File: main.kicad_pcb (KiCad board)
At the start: 2 copper layers, 228.6 x 70.6 mm, 132 parts, among them J1 Conn_02x16_Row_Letter_First, J2 Conn_01x06, J3 Conn_01x02, J4 Screw_Terminal_01x02, J5 Screw_Terminal_01x10, J6 Screw_Terminal_01x10, J7 Screw_Terminal_01x02, J8 Screw_Terminal_01x10, J9 Screw_Terminal_01x10, U1 TPS73233DBVR, U10 TLP222A, U11 TLP222A, U12 TLP222A, U13 TLP222A, U14 TLP222A, U15 TLP222A, U16 TLP222A, U17 TLP222A, U18 TLP222A, U19 TLP222A, U20 TLP222A, U21 TLP222A, U22 TLP222A, U23 TLP222A, U24 TLP222A, U25 TLP222A, U26 TLP3558A, U27 TLP3558A, U28 TLP222A, U29 TLP222A, U3 STM32G070xB, U30 TLP222A, U31 TLP222A, U32 TLP222A, U33 TLP222A, U34 TLP222A, U35 TLP222A, U36 TLP222A, U37 TLP222A, U38 TLP222A, U39 TLP222A, U4 TLP222A, U40 TLP222A, U41 TLP222A, U42 TLP222A, U43 TLP222A, U44 TLP222A, U45 TLP222A, U46 TLP222A, U47 TLP222A, U5 TLP222A, U6 TLP222A, U7 TLP222A, U8 TLP222A, U9 TLP222A

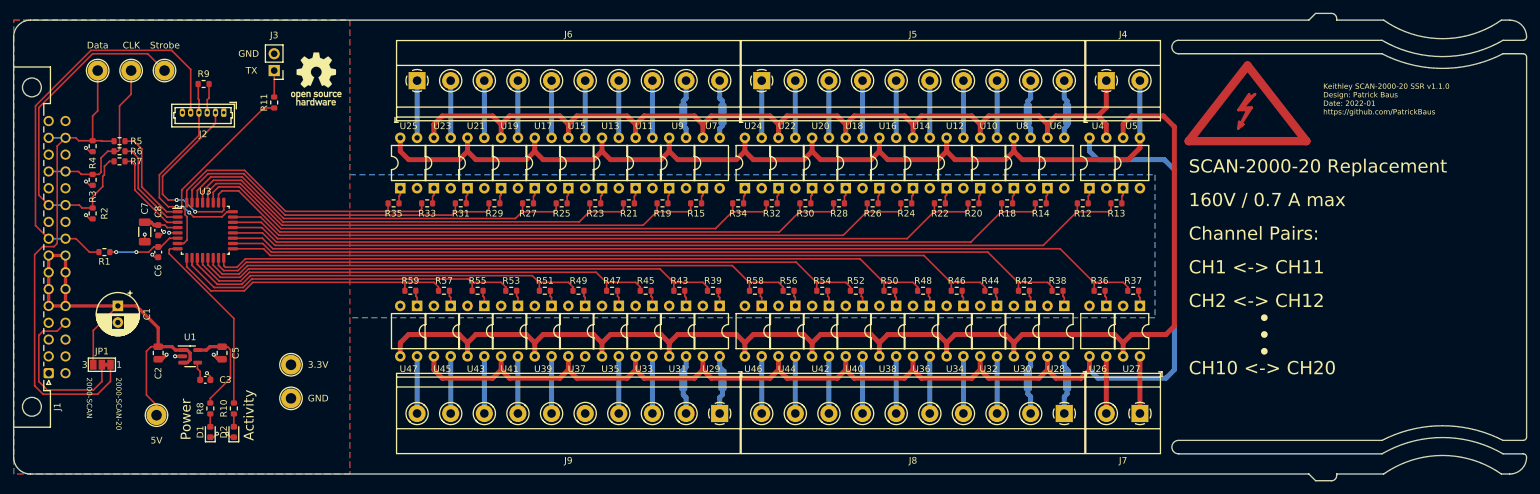
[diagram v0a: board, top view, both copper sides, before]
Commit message: Replaced Picoblade connector with standard pin header Updated libraries to KiCAD 6 format
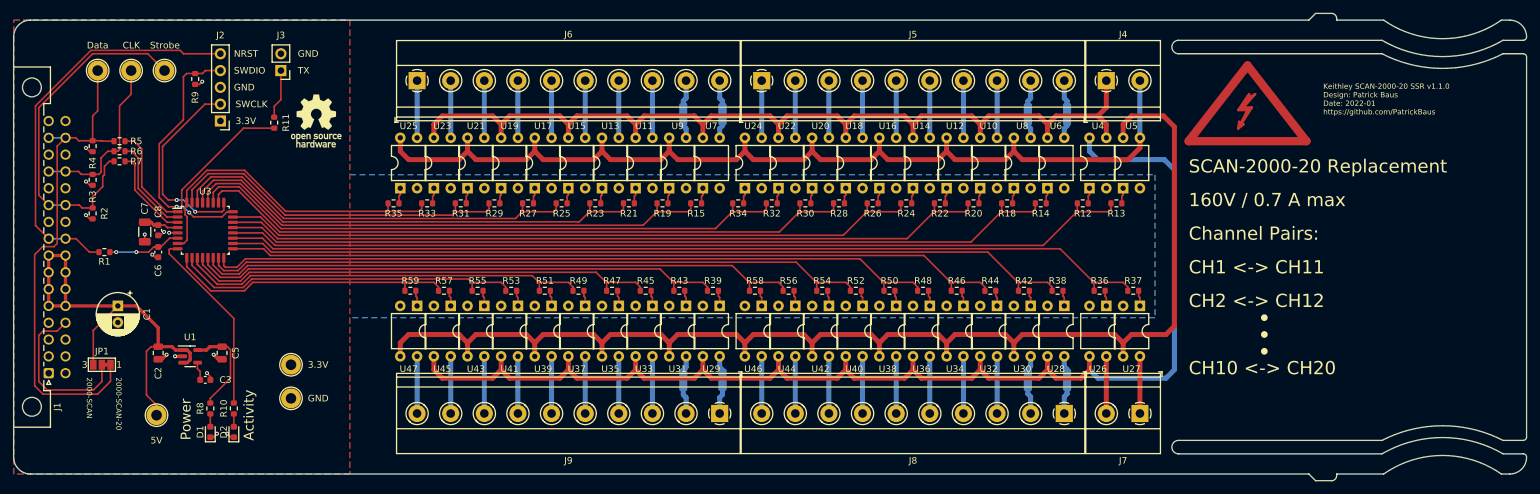
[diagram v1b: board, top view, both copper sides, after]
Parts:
- J2: value Conn_01x06 -> Conn_01x05; footprint Connector_Molex:Molex_PicoBlade_53047-0610_1x06_P1.25mm_Vertical -> Connector_PinHeader_2.54mm:PinHeader_1x05_P2.54mm_Vertical
- moved LOGO2 6.35 mm to (71.1, 63.5)
- moved R11 3.05 mm to (64.8, 63.8)
- moved R9 1.48 mm to (52.8, 57.1), turned to -90 degrees
- moved J2 1.37 mm to (56.6, 63.5)
- moved J3 1.02 mm to (65.8, 55.9)
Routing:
- net Net-(J9-Pad5): track 0.00 -> 8.64 mm
- net /Microcontroller/SWDIO: track 32.3 -> 38.4 mm
- net Net-(J3-Pad1): track 4.00 -> 7.47 mm
- net GND: track 20.7 -> 17.6 mm, vias 13 -> 14
- net /~{NRST}: track 64.0 -> 61.0 mm
- net /Microcontroller/SWCLK: track 27.2 -> 30.2 mm
- net /Microcontroller/TX: track 28.6 -> 27.4 mm
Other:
- board text added: "NRST"
- board text added: "SWCLK"
- board text added: "SWDIO"

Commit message: Updated silkscreen
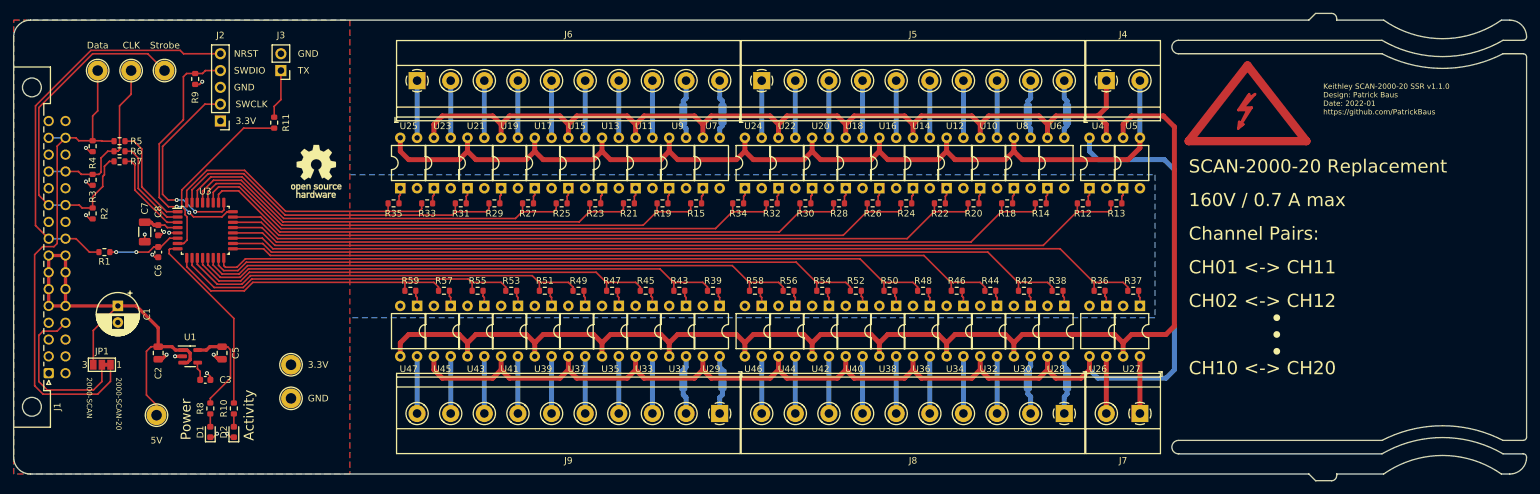
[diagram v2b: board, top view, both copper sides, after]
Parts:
- U3: value STM32G070xB -> STM32G070KBT6
- moved LOGO2 7.62 mm to (71.1, 71.1)
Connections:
- net /Relays/Input pins/In_HIGH renamed /Relays/Input pins/Out_HIGH
- net /Relays/Input pins/In_LOW renamed /Relays/Input pins/Out_LOW
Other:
- board text added: "CH01 <-> CH11"
- board text added: "CH02 <-> CH12"
- board text removed: "CH1 <-> CH11"
- board text removed: "CH2 <-> CH12"

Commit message: Updated BOM
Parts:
- U10, U11, U12, U13, U14, U15, U16, U17, U18, U19, U20, U21, U22, U23, U24, U25, U28, U29, U30, U31, U32, U33, U34, U35, U36, U37, U38, U39, U4, U40, U41, U42, U43, U44, U45, U46, U47, U5, U6, U7, U8, U9: value TLP222A -> TLP3558A

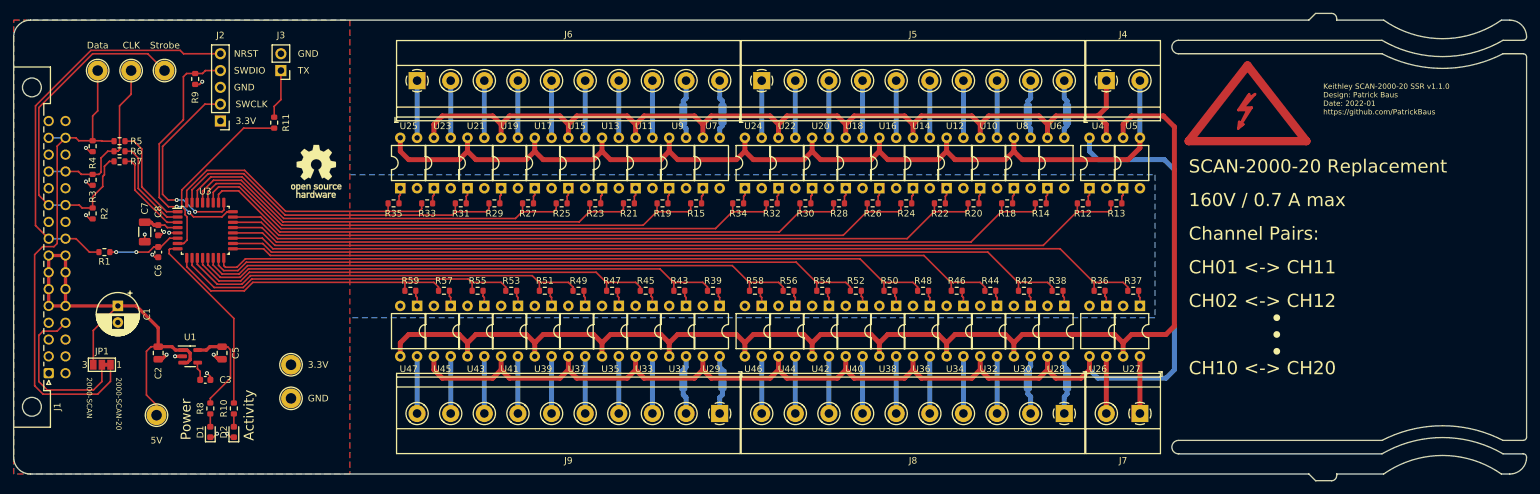
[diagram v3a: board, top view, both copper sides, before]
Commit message: Updated to KiCad 8 (#1)
- Updated libraries
- Updated BOM, replaced obsolete parts
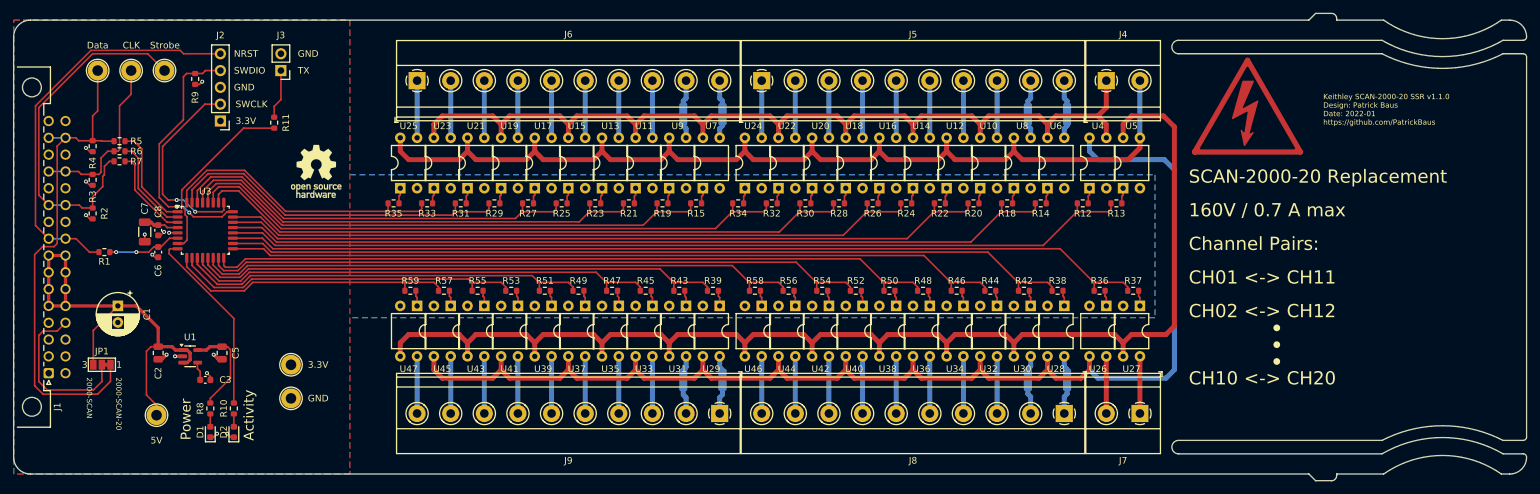
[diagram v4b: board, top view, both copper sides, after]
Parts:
- SYM1: footprint Symbol:Symbol_Highvoltage_Type2_CopperTop_Small -> Symbol:Symbol_HighVoltage_Triangle_17x15mm_Copper
- moved SYM1 1.48 mm to (211.8, 61.3)
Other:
- board text added: "1.5 mm"
- board text added: "35 µm"
- board text added: "Copper"
- board text added: "Core"
- board text added: "Manufacturing Instruction: - Material FR-4 - Finished thickness: 1.57 mm ± 0.13 mm - Surface finish: ENIG - Solder mask color: Green - PCBs are to be RoHS compliant - Do not edit artwork, e.g. to add logos or order numbers - Clean to meet IPC J-STD-001E, Class 2 after assembly"
- board text added: "Material"
- board text added: "Stackup:"
- board text added: "Thickness"
- board text removed: "Manufacturing Instruction: - Material FR-4 - Finished thickness: 1.57 mm ± 0.13 mm - Surface finish: ENIG - Solder mask color: Blue - PCBs are to be RoHS compliant - Do not edit artwork, e.g. to add logos or order numbers - Clean to meet IPC J-STD-001E, Class 2 after assembly"
